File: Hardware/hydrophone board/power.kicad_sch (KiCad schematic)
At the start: 19 parts, among them J10 Conn_01x03, U5 LT1963AxST-3.3

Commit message: Revert "Merge branch 'hardware' of https://github.com/bruin-underwater-robotics/2023-2024 into hardware"
This reverts commit 1d5f0f31a35e539c7b0b2eac7ff2db3bf82506a7, reversing
changes made to b9b3862216192341382b87943b4a1d0c2c46b631.
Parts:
- removed J10: Conn_01x03, symbol Connector_Generic:Conn_01x03
- added J203: Screw_Terminal_01x02, symbol Connector:Screw_Terminal_01x02
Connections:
- net +3.3VA: now also U5.3 (OUT)
- net +5V: now also J203.1 (Pin_1)
- net GND: now also J203.2 (Pin_2)
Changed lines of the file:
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@@
+    (stroke (width 0) (type default))
+  )
+  (wire (pts (xy 39.37 100.33) (xy 39.37 102.87))
     (stroke (width 0) (type default))
   )
@@
     (stroke (width 0) (type default))
   )
+  (wire (pts (xy 39.37 105.41) (xy 39.37 107.95))
+    (stroke (width 0) (type default))
+  )
   (wire (pts (xy 120.65 139.7) (xy 125.73 139.7))
     (stroke (width 0) (type default))
@@
     (stroke (width 0) (type default))
   )
-  (wire (pts (xy 152.4 76.2) (xy 144.78 76.2))
-    (stroke (width 0) (type default))
-  )
   (wire (pts (xy 180.34 76.2) (xy 190.5 76.2))
     (stroke (width 0) (type default))
@@
     (stroke (width 0) (type default))
   )
+  (wire (pts (xy 137.16 76.2) (xy 152.4 76.2))
+    (stroke (width 0) (type default))
+  )
   (wire (pts (xy 120.65 127) (xy 125.73 127))
     (stroke (width 0) (type default))
@@
     (stroke (width 0) (type default))
   )
-  (wire (pts (xy 142.24 54.61) (xy 142.24 76.2))
-    (stroke (width 0) (type default))
-  )
   (wire (pts (xy 101.6 76.2) (xy 101.6 81.28))
     (stroke (width 0) (type default))
@@
     (stroke (width 0) (type default))
   )
-  (wire (pts (xy 144.78 76.2) (xy 144.78 54.61))
-    (stroke (width 0) (type default))
-  )
   (wire (pts (xy 190.5 72.39) (xy 190.5 76.2))
     (stroke (width 0) (type default))
@@
     (stroke (width 0) (type default))
   )
-  (wire (pts (xy 137.16 76.2) (xy 142.24 76.2))
-    (stroke (width 0) (type default))
-  )
   (wire (pts (xy 88.9 72.39) (xy 88.9 76.2))
     (stroke (width 0) (type default))
@@
   )
   (wire (pts (xy 139.7 152.4) (xy 139.7 157.48))
-    (stroke (width 0) (type default))
-  )
-  (wire (pts (xy 147.32 54.61) (xy 147.32 57.15))
     (stroke (width 0) (type default))
   )
@@
     (effects (font (size 1.27 1.27)) (justify left bottom))
   )
-  (hierarchical_label "3.3V MCU" (shape input) (at 147.32 57.15 270) (fields_autoplaced)
-    (effects (font (size 1.27 1.27)) (justify right))
-  )
   (symbol (lib_id "Connector:TestPoint_Probe") (at 152.4 76.2 0) (unit 1)
     (in_bom yes) (on_board yes) (dnp no) (fields_autoplaced)
@@
         (path "/4356d3a6-6a00-447d-897e-473f60221539/cf9d259f-9643-49eb-8aca-1ca8b75f4d64"
           (reference "L1") (unit 1)
+        )
+      )
+    )
+  )
+  (symbol (lib_id "power:+5V") (at 39.37 100.33 0) (unit 1)
+    (in_bom yes) (on_board yes) (dnp no) (fields_autoplaced)
+    (property "Reference" "#PWR0202" (at 39.37 104.14 0)
+      (effects (font (size 1.27 1.27)) hide)
+    )
+    (property "Value" "+5V" (at 39.37 96.52 0)
+      (effects (font (size 1.27 1.27)))
+    )
+    (property "Footprint" "" (at 39.37 100.33 0)
+      (effects (font (size 1.27 1.27)) hide)
+    )
+    (property "Datasheet" "" (at 39.37 100.33 0)
+      (effects (font (size 1.27 1.27)) hide)
+    )
+    (pin "1")
+    (instances
+      (project "hydrophone board"
+        (path "/4356d3a6-6a00-447d-897e-473f60221539/1cfbaf71-7039-4355-8fc7-d8c77f0e8058"
+          (reference "#PWR0202") (unit 1)
+        )
+        (path "/4356d3a6-6a00-447d-897e-473f60221539/cf9d259f-9643-49eb-8aca-1ca8b75f4d64"
+          (reference "#PWR030") (unit 1)
         )
       )
@@
     )
   )
+  (symbol (lib_id "power:GND") (at 39.37 107.95 0) (unit 1)
+    (in_bom yes) (on_board yes) (dnp no) (fields_autoplaced)
+    (property "Reference" "#PWR0201" (at 39.37 114.3 0)
+      (effects (font (size 1.27 1.27)) hide)
+    )
+    (property "Value" "GND" (at 39.37 113.03 0)
+      (effects (font (size 1.27 1.27)))
+    )
+    (property "Footprint" "" (at 39.37 107.95 0)
+      (effects (font (size 1.27 1.27)) hide)
+    )
+    (property "Datasheet" "" (at 39.37 107.95 0)
+      (effects (font (size 1.27 1.27)) hide)
+    )
+    (pin "1")
+    (instances
+      (project "hydrophone board"
+        (path "/4356d3a6-6a00-447d-897e-473f60221539/1cfbaf71-7039-4355-8fc7-d8c77f0e8058"
+          (reference "#PWR0201") (unit 1)
+        )
+        (path "/4356d3a6-6a00-447d-897e-473f60221539/cf9d259f-9643-49eb-8aca-1ca8b75f4d64"
+          (reference "#PWR031") (unit 1)
+        )
+      )
+    )
+  )
   (symbol (lib_id "power:+5V") (at 107.95 127 90) (unit 1)
     (in_bom yes) (on_board yes) (dnp no) (fields_autoplaced)
@@
     )
   )
-  (symbol (lib_id "Connector_Generic:Conn_01x03") (at 144.78 49.53 90) (unit 1)
-    (in_bom yes) (on_board yes) (dnp no) (fields_autoplaced)
-    (property "Reference" "J10" (at 149.86 48.26 90)
-      (effects (font (size 1.27 1.27)) (justify right))
-    )
-    (property "Value" "Conn_01x03" (at 149.86 50.8 90)
-      (effects (font (size 1.27 1.27)) (justify right))
-    )
-    (property "Footprint" "" (at 144.78 49.53 0)
-      (effects (font (size 1.27 1.27)) hide)
-    )
-    (property "Datasheet" "~" (at 144.78 49.53 0)
-      (effects (font (size 1.27 1.27)) hide)
-    )
-    (pin "1")
-    (pin "2")
-    (pin "3")
-    (instances
-      (project "hydrophone board"
-        (path "/4356d3a6-6a00-447d-897e-473f60221539/cf9d259f-9643-49eb-8aca-1ca8b75f4d64"
-          (reference "J10") (unit 1)
-        )
-      )
-    )
-  )
   (symbol (lib_id "Device:LED") (at 116.84 127 180) (unit 1)
     (in_bom yes) (on_board yes) (dnp no) (fields_autoplaced)
@@
         )
       )
+    )
+  )
+  (symbol (lib_id "Connector:Screw_Terminal_01x02") (at 44.45 102.87 0) (unit 1)
+    (in_bom yes) (on_board yes) (dnp no) (fields_autoplaced)
+    (property "Reference" "J203" (at 46.99 103.505 0)
+      (effects (font (size 1.27 1.27)) (justify left))
+    )
+    (property "Value" "Screw_Terminal_01x02" (at 46.99 106.045 0)
+      (effects (font (size 1.27 1.27)) (justify left))
+    )
+    (property "Footprint" "" (at 44.45 102.87 0)
+      (effects (font (size 1.27 1.27)) hide)
+    )
+    (property "Datasheet" "~" (at 44.45 102.87 0)
+      (effects (font (size 1.27 1.27)) hide)
+    )
+    (pin "1")
+    (pin "2")
+    (instances
+      (project "hydrophone board"
+        (path "/4356d3a6-6a00-447d-897e-473f60221539/1cfbaf71-7039-4355-8fc7-d8c77f0e8058"
+          (reference "J203") (unit 1)
+        )
+        (path "/4356d3a6-6a00-447d-897e-473f60221539/cf9d259f-9643-49eb-8aca-1ca8b75f4d64"
+          (reference "J11") (unit 1)
+        )
+      )

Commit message: 3.3v connector
on power sheet
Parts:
- added J10: Conn_01x03, symbol Connector_Generic:Conn_01x03
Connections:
- net +3.3VA: now also J10.2 (Pin_2); no longer U5.3 (OUT)
- new net: J10.1 (Pin_1), U5.3 (OUT)
- new net 3.3V MCU: J10.3 (Pin_3)
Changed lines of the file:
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@@
+    (stroke (width 0) (type default))
+  )
+  (wire (pts (xy 152.4 76.2) (xy 144.78 76.2))
     (stroke (width 0) (type default))
   )
@@
     (stroke (width 0) (type default))
   )
-  (wire (pts (xy 137.16 76.2) (xy 152.4 76.2))
-    (stroke (width 0) (type default))
-  )
   (wire (pts (xy 120.65 127) (xy 125.73 127))
     (stroke (width 0) (type default))
@@
     (stroke (width 0) (type default))
   )
+  (wire (pts (xy 142.24 54.61) (xy 142.24 76.2))
+    (stroke (width 0) (type default))
+  )
   (wire (pts (xy 101.6 76.2) (xy 101.6 81.28))
     (stroke (width 0) (type default))
@@
     (stroke (width 0) (type default))
   )
+  (wire (pts (xy 144.78 76.2) (xy 144.78 54.61))
+    (stroke (width 0) (type default))
+  )
   (wire (pts (xy 190.5 72.39) (xy 190.5 76.2))
     (stroke (width 0) (type default))
@@
     (stroke (width 0) (type default))
   )
+  (wire (pts (xy 137.16 76.2) (xy 142.24 76.2))
+    (stroke (width 0) (type default))
+  )
   (wire (pts (xy 88.9 72.39) (xy 88.9 76.2))
     (stroke (width 0) (type default))
@@
   )
   (wire (pts (xy 139.7 152.4) (xy 139.7 157.48))
+    (stroke (width 0) (type default))
+  )
+  (wire (pts (xy 147.32 54.61) (xy 147.32 57.15))
     (stroke (width 0) (type default))
   )
@@
     (effects (font (size 1.27 1.27)) (justify left bottom))
   )
+  (hierarchical_label "3.3V MCU" (shape input) (at 147.32 57.15 270) (fields_autoplaced)
+    (effects (font (size 1.27 1.27)) (justify right))
+  )
   (symbol (lib_id "Connector:TestPoint_Probe") (at 152.4 76.2 0) (unit 1)
     (in_bom yes) (on_board yes) (dnp no) (fields_autoplaced)
@@
         )
       )
+    )
+  )
+  (symbol (lib_id "Connector_Generic:Conn_01x03") (at 144.78 49.53 90) (unit 1)
+    (in_bom yes) (on_board yes) (dnp no) (fields_autoplaced)
+    (property "Reference" "J10" (at 149.86 48.26 90)
+      (effects (font (size 1.27 1.27)) (justify right))
+    )
+    (property "Value" "Conn_01x03" (at 149.86 50.8 90)
+      (effects (font (size 1.27 1.27)) (justify right))
+    )
+    (property "Footprint" "" (at 144.78 49.53 0)
+      (effects (font (size 1.27 1.27)) hide)
+    )
+    (property "Datasheet" "~" (at 144.78 49.53 0)
+      (effects (font (size 1.27 1.27)) hide)
+    )
+    (pin "1")
+    (pin "2")
+    (pin "3")
+    (instances
+      (project "hydrophone board"
+        (path "/4356d3a6-6a00-447d-897e-473f60221539/cf9d259f-9643-49eb-8aca-1ca8b75f4d64"
+          (reference "J10") (unit 1)
+        )
+      )

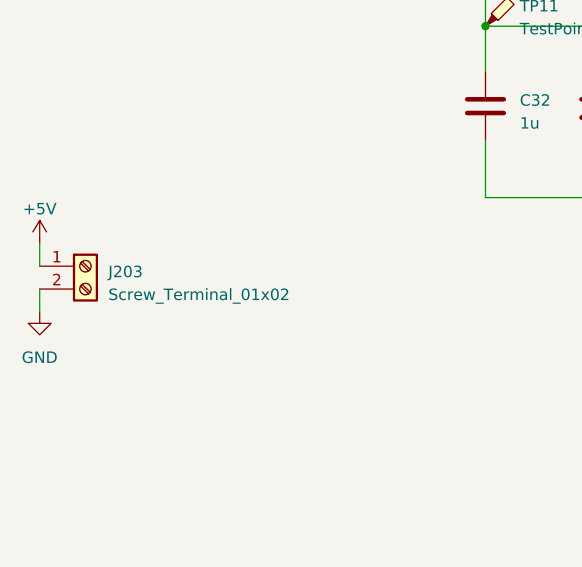
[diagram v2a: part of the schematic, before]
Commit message: added ds_store to gitignore
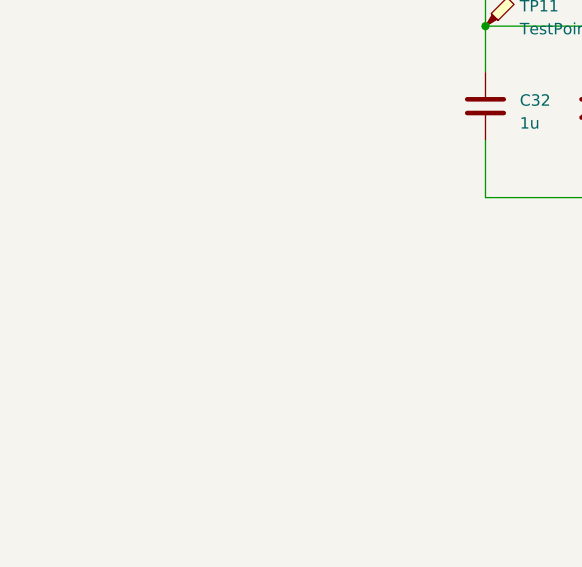
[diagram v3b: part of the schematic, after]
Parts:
- removed J203: Screw_Terminal_01x02, symbol Connector:Screw_Terminal_01x02
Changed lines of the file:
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@@
-    (stroke (width 0) (type default))
-  )
-  (wire (pts (xy 39.37 100.33) (xy 39.37 102.87))
     (stroke (width 0) (type default))
   )
@@
   )
   (wire (pts (xy 139.7 139.7) (xy 139.7 152.4))
-    (stroke (width 0) (type default))
-  )
-  (wire (pts (xy 39.37 105.41) (xy 39.37 107.95))
     (stroke (width 0) (type default))
   )
@@
     )
   )
-  (symbol (lib_id "power:+5V") (at 39.37 100.33 0) (unit 1)
-    (in_bom yes) (on_board yes) (dnp no) (fields_autoplaced)
-    (property "Reference" "#PWR0202" (at 39.37 104.14 0)
-      (effects (font (size 1.27 1.27)) hide)
-    )
-    (property "Value" "+5V" (at 39.37 96.52 0)
-      (effects (font (size 1.27 1.27)))
-    )
-    (property "Footprint" "" (at 39.37 100.33 0)
-      (effects (font (size 1.27 1.27)) hide)
-    )
-    (property "Datasheet" "" (at 39.37 100.33 0)
-      (effects (font (size 1.27 1.27)) hide)
-    )
-    (pin "1")
-    (instances
-      (project "hydrophone board"
-        (path "/4356d3a6-6a00-447d-897e-473f60221539/1cfbaf71-7039-4355-8fc7-d8c77f0e8058"
-          (reference "#PWR0202") (unit 1)
-        )
-        (path "/4356d3a6-6a00-447d-897e-473f60221539/cf9d259f-9643-49eb-8aca-1ca8b75f4d64"
-          (reference "#PWR030") (unit 1)
-        )
-      )
-    )
-  )
   (symbol (lib_id "power:+3.3VA") (at 107.95 139.7 90) (unit 1)
     (in_bom yes) (on_board yes) (dnp no) (fields_autoplaced)
@@
     )
   )
-  (symbol (lib_id "power:GND") (at 39.37 107.95 0) (unit 1)
-    (in_bom yes) (on_board yes) (dnp no) (fields_autoplaced)
-    (property "Reference" "#PWR0201" (at 39.37 114.3 0)
-      (effects (font (size 1.27 1.27)) hide)
-    )
-    (property "Value" "GND" (at 39.37 113.03 0)
-      (effects (font (size 1.27 1.27)))
-    )
-    (property "Footprint" "" (at 39.37 107.95 0)
-      (effects (font (size 1.27 1.27)) hide)
-    )
-    (property "Datasheet" "" (at 39.37 107.95 0)
-      (effects (font (size 1.27 1.27)) hide)
-    )
-    (pin "1")
-    (instances
-      (project "hydrophone board"
-        (path "/4356d3a6-6a00-447d-897e-473f60221539/1cfbaf71-7039-4355-8fc7-d8c77f0e8058"
-          (reference "#PWR0201") (unit 1)
-        )
-        (path "/4356d3a6-6a00-447d-897e-473f60221539/cf9d259f-9643-49eb-8aca-1ca8b75f4d64"
-          (reference "#PWR031") (unit 1)
-        )
-      )
-    )
-  )
   (symbol (lib_id "power:+5V") (at 107.95 127 90) (unit 1)
     (in_bom yes) (on_board yes) (dnp no) (fields_autoplaced)
@@
         )
       )
-    )
-  )
-  (symbol (lib_id "Connector:Screw_Terminal_01x02") (at 44.45 102.87 0) (unit 1)
-    (in_bom yes) (on_board yes) (dnp no) (fields_autoplaced)
-    (property "Reference" "J203" (at 46.99 103.505 0)
-      (effects (font (size 1.27 1.27)) (justify left))
-    )
-    (property "Value" "Screw_Terminal_01x02" (at 46.99 106.045 0)
-      (effects (font (size 1.27 1.27)) (justify left))
-    )
-    (property "Footprint" "" (at 44.45 102.87 0)
-      (effects (font (size 1.27 1.27)) hide)
-    )
-    (property "Datasheet" "~" (at 44.45 102.87 0)
-      (effects (font (size 1.27 1.27)) hide)
-    )
-    (pin "1")
-    (pin "2")
-    (instances
-      (project "hydrophone board"
-        (path "/4356d3a6-6a00-447d-897e-473f60221539/1cfbaf71-7039-4355-8fc7-d8c77f0e8058"
-          (reference "J203") (unit 1)
-        )
-        (path "/4356d3a6-6a00-447d-897e-473f60221539/cf9d259f-9643-49eb-8aca-1ca8b75f4d64"
-          (reference "J11") (unit 1)
-        )
-      )
